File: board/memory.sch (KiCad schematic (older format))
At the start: 6 parts, among them U12 AS6C4008, U13 AS6C4008, U14 W29C020C

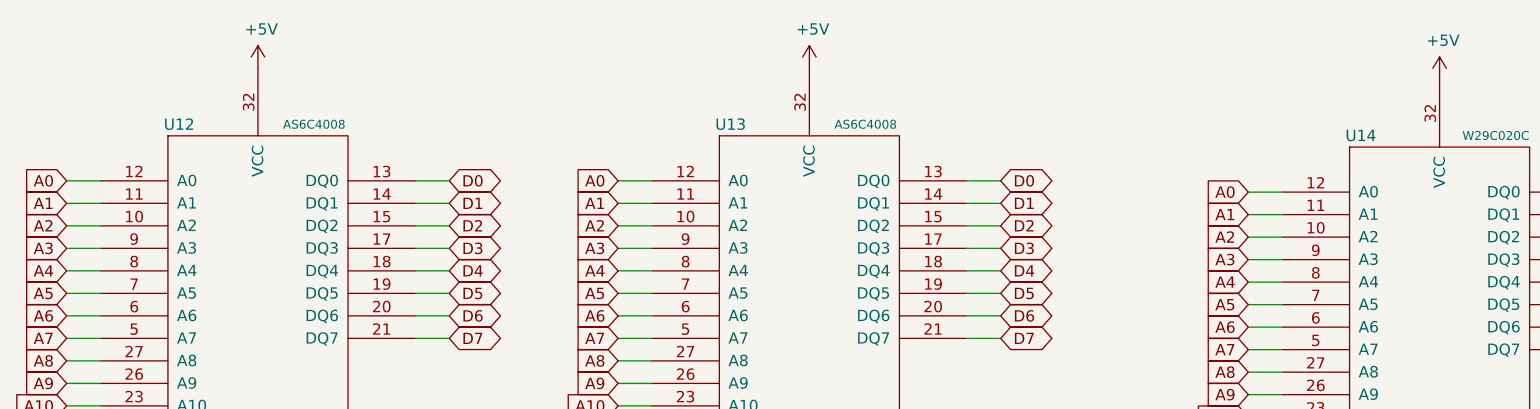
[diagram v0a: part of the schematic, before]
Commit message: RC1 of schematic and initial board layout
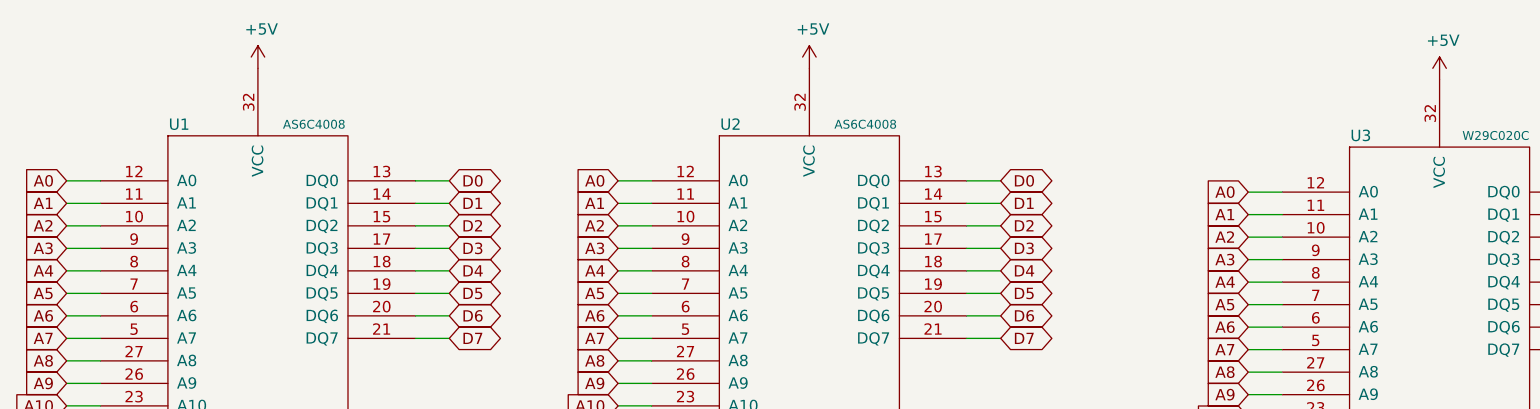
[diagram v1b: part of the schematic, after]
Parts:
- C1: renamed from C23; value 1u -> 0.1u; footprint (none) -> Capacitor_THT:C_Rect_L4.6mm_W2.0mm_P2.50mm_MKS02_FKP02
- C2: renamed from C24; value 1u -> 0.1u; footprint (none) -> Capacitor_THT:C_Rect_L4.6mm_W2.0mm_P2.50mm_MKS02_FKP02
- C3: renamed from C25; value 1u -> 0.1u; footprint (none) -> Capacitor_THT:C_Rect_L4.6mm_W2.0mm_P2.50mm_MKS02_FKP02
- U3: renamed from U14; footprint Package_DIP:DIP-32_W15.24mm -> Socket:DIP_Socket-32_W11.9_W12.7_W15.24_W17.78_W18.5_3M_232-1285-00-0602J
- renumbered U12 to U1, U13 to U2
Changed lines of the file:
@@
 $Descr USLetter 11000 8500
 encoding utf-8
-Sheet 5 8
+Sheet 2 7
 Title "JRC-1 RAM and ROM"
 Date "2021-12-04"
@@
 $EndDescr
 $Comp
-L Memory:AS6C4008 U12
+L Memory:AS6C4008 U1
 U 1 1 61ADEFE1
 P 2950 3950
-F 0 "U12" H 2600 5100 50  0000 C CNN
+F 0 "U1" H 2600 5100 50  0000 C CNN
 F 1 "AS6C4008" H 3200 5100 39  0000 C CNN
 F 2 "Package_DIP:DIP-32_W15.24mm" H 2900 5600 50  0001 C CNN
@@
 	3650 3750 3800 3750
 $Comp
-L power:+5V #PWR035
+L power:+5V #PWR03
 U 1 1 61B0ED14
 P 2950 2550
-F 0 "#PWR035" H 2950 2400 50  0001 C CNN
+F 0 "#PWR03" H 2950 2400 50  0001 C CNN
 F 1 "+5V" H 2965 2723 50  0000 C CNN
 F 2 "" H 2950 2550 50  0001 C CNN
@@
 $EndComp
 $Comp
-L power:GND #PWR036
+L power:GND #PWR04
 U 1 1 61B10976
 P 2950 5350
-F 0 "#PWR036" H 2950 5100 50  0001 C CNN
+F 0 "#PWR04" H 2950 5100 50  0001 C CNN
 F 1 "GND" H 2955 5177 50  0000 C CNN
 F 2 "" H 2950 5350 50  0001 C CNN
@@
 $EndComp
 $Comp
-L Memory:AS6C4008 U13
+L Memory:AS6C4008 U2
 U 1 1 61B14B22
 P 5400 3950
-F 0 "U13" H 5050 5100 50  0000 C CNN
+F 0 "U2" H 5050 5100 50  0000 C CNN
 F 1 "AS6C4008" H 5650 5100 39  0000 C CNN
 F 2 "Package_DIP:DIP-32_W15.24mm" H 5350 5600 50  0001 C CNN
@@
 	6100 3750 6250 3750
 $Comp
-L power:+5V #PWR037
+L power:+5V #PWR05
 U 1 1 61B14B64
 P 5400 2550
-F 0 "#PWR037" H 5400 2400 50  0001 C CNN
+F 0 "#PWR05" H 5400 2400 50  0001 C CNN
 F 1 "+5V" H 5415 2723 50  0000 C CNN
 F 2 "" H 5400 2550 50  0001 C CNN
@@
 $EndComp
 $Comp
-L power:GND #PWR038
+L power:GND #PWR06
 U 1 1 61B14B6A
 P 5400 5350
-F 0 "#PWR038" H 5400 5100 50  0001 C CNN
+F 0 "#PWR06" H 5400 5100 50  0001 C CNN
 F 1 "GND" H 5405 5177 50  0000 C CNN
 F 2 "" H 5400 5350 50  0001 C CNN
@@
 $EndComp
 $Comp
-L Memory:W29C020C U14
+L Memory:W29C020C U3
 U 1 1 61B194BA
 P 8200 4000
-F 0 "U14" H 7850 5150 50  0000 C CNN
+F 0 "U3" H 7850 5150 50  0000 C CNN
 F 1 "W29C020C" H 8450 5150 39  0000 C CNN
-F 2 "Package_DIP:DIP-32_W15.24mm" H 8150 5650 50  0001 C CNN
+F 2 "Socket:DIP_Socket-32_W11.9_W12.7_W15.24_W17.78_W18.5_3M_232-1285-00-0602J" H 8150 5650 50  0001 C CNN
 F 3 "" H 8200 4000 50  0001 C CNN
 	1    8200 4000
@@
 A0
 $Comp
-L power:GND #PWR040
+L power:GND #PWR08
 U 1 1 61B29161
 P 8200 5400
-F 0 "#PWR040" H 8200 5150 50  0001 C CNN
+F 0 "#PWR08" H 8200 5150 50  0001 C CNN
 F 1 "GND" H 8205 5227 50  0000 C CNN
 F 2 "" H 8200 5400 50  0001 C CNN
@@
 P 1200 7650
 AR Path="/60EE1618/61F0D492" Ref="#PWR?"  Part="1"
-AR Path="/61ADDFAC/61F0D492" Ref="#PWR034"  Part="1"
-F 0 "#PWR034" H 1200 7400 50  0001 C CNN
+AR Path="/61ADDFAC/61F0D492" Ref="#PWR02"  Part="1"
+F 0 "#PWR02" H 1200 7400 50  0001 C CNN
 F 1 "GND" H 1205 7477 50  0000 C CNN
 F 2 "" H 1200 7650 50  0001 C CNN
@@
 P 800 7350
 AR Path="/60EE1618/61F0D498" Ref="C?"  Part="1"
-AR Path="/61ADDFAC/61F0D498" Ref="C23"  Part="1"
-F 0 "C23" H 892 7396 50  0001 L CNN
-F 1 "1u" H 892 7350 50  0001 L CNN
-F 2 "" H 800 7350 50  0001 C CNN
+AR Path="/61ADDFAC/61F0D498" Ref="C1"  Part="1"
+F 0 "C1" H 892 7396 50  0001 L CNN
+F 1 "0.1u" H 892 7350 50  0001 L CNN
+F 2 "Capacitor_THT:C_Rect_L4.6mm_W2.0mm_P2.50mm_MKS02_FKP02" H 800 7350 50  0001 C CNN
 F 3 "~" H 800 7350 50  0001 C CNN
 	1    800  7350
@@
 P 800 7050
 AR Path="/60EE1618/61F0D49E" Ref="#PWR?"  Part="1"
-AR Path="/61ADDFAC/61F0D49E" Ref="#PWR033"  Part="1"
-F 0 "#PWR033" H 800 6900 50  0001 C CNN
+AR Path="/61ADDFAC/61F0D49E" Ref="#PWR01"  Part="1"
+F 0 "#PWR01" H 800 6900 50  0001 C CNN
 F 1 "+5V" H 815 7223 50  0000 C CNN
 F 2 "" H 800 7050 50  0001 C CNN
@@
 P 1000 7350
 AR Path="/60EE1618/61F0D4A4" Ref="C?"  Part="1"
-AR Path="/61ADDFAC/61F0D4A4" Ref="C24"  Part="1"
-F 0 "C24" H 1092 7396 50  0001 L CNN
-F 1 "1u" H 1092 7350 50  0001 L CNN
-F 2 "" H 1000 7350 50  0001 C CNN
+AR Path="/61ADDFAC/61F0D4A4" Ref="C2"  Part="1"
+F 0 "C2" H 1092 7396 50  0001 L CNN
+F 1 "0.1u" H 1092 7350 50  0001 L CNN
+F 2 "Capacitor_THT:C_Rect_L4.6mm_W2.0mm_P2.50mm_MKS02_FKP02" H 1000 7350 50  0001 C CNN
 F 3 "~" H 1000 7350 50  0001 C CNN
 	1    1000 7350
@@
 P 1200 7350
 AR Path="/60EE1618/61F0D4AA" Ref="C?"  Part="1"
-AR Path="/61ADDFAC/61F0D4AA" Ref="C25"  Part="1"
-F 0 "C25" H 1292 7396 50  0001 L CNN
-F 1 "1u" H 1292 7350 50  0001 L CNN
-F 2 "" H 1200 7350 50  0001 C CNN
+AR Path="/61ADDFAC/61F0D4AA" Ref="C3"  Part="1"
+F 0 "C3" H 1292 7396 50  0001 L CNN
+F 1 "0.1u" H 1292 7350 50  0001 L CNN
+F 2 "Capacitor_THT:C_Rect_L4.6mm_W2.0mm_P2.50mm_MKS02_FKP02" H 1200 7350 50  0001 C CNN
 F 3 "~" H 1200 7350 50  0001 C CNN
 	1    1200 7350
@@
 Connection ~ 1200 7550
 $Comp
-L power:+5V #PWR039
+L power:+5V #PWR07
 U 1 1 61D1FEE9
 P 8200 2600
-F 0 "#PWR039" H 8200 2450 50  0001 C CNN
+F 0 "#PWR07" H 8200 2450 50  0001 C CNN
 F 1 "+5V" H 8215 2773 50  0000 C CNN
 F 2 "" H 8200 2600 50  0001 C CNN

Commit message: RC1 of schematic and initial board layout
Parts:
- U1, U2: footprint Package_DIP:DIP-32_W15.24mm -> Package_DIP:DIP-32_W15.24mm_Socket
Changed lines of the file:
@@
 F 0 "U1" H 2600 5100 50  0000 C CNN
 F 1 "AS6C4008" H 3200 5100 39  0000 C CNN
-F 2 "Package_DIP:DIP-32_W15.24mm" H 2900 5600 50  0001 C CNN
+F 2 "Package_DIP:DIP-32_W15.24mm_Socket" H 2900 5600 50  0001 C CNN
 F 3 "" H 2950 3950 50  0001 C CNN
 	1    2950 3950
@@
 F 0 "U2" H 5050 5100 50  0000 C CNN
 F 1 "AS6C4008" H 5650 5100 39  0000 C CNN
-F 2 "Package_DIP:DIP-32_W15.24mm" H 5350 5600 50  0001 C CNN
+F 2 "Package_DIP:DIP-32_W15.24mm_Socket" H 5350 5600 50  0001 C CNN
 F 3 "" H 5400 3950 50  0001 C CNN
 	1    5400 3950
